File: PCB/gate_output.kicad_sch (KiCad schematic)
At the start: 7 parts

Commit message: :sparkles: Add the counter logic
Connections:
- net GATE_OUT: no longer D?.2 (A)
- net at Q?.3 (E), R?.1, R?.2: now also D?.2 (A)
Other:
- moved on the sheet: D?, R?

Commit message: :wrench: Set CLIFF footprints for the jacks
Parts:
- J?: footprint moPsy:Jack_3.5mm_QingPu_WQP-PJ398SM_Vertical_CircularHoles_Centered -> moPsy:CLIFF 3.5mm S6 Mono Jack Socket
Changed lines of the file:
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@@
       (effects (font (size 1.27 1.27)) (justify right))
     )
-    (property "Footprint" "moPsy:Jack_3.5mm_QingPu_WQP-PJ398SM_Vertical_CircularHoles_Centered" (at 92.075 63.5 0)
+    (property "Footprint" "moPsy:CLIFF 3.5mm S6 Mono Jack Socket" (at 92.075 63.5 0)
       (effects (font (size 1.27 1.27)) hide)
     )

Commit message: :wrench: Adjust project name on sheets
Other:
- company: (none) -> moPsy
- title: (none) -> DIV
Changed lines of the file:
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@@
 (kicad_sch (version 20230121) (generator eeschema)
   (paper "A4")
+  (title_block
+    (title "DIV")
+    (date "2023-04-03")
+    (rev "v1")
+    (company "moPsy")
+  )
   (junction (at 66.675 55.245) (diameter 0) (color 0 0 0 0)
   )
@@
         )
       )
-      (project "the-count"
+      (project "div"
         (path "/69636855-5bea-4b1f-bae0-d5724c7c5e69"
           (reference "Q?") (unit 1)
@@
         )
       )
-      (project "the-count"
+      (project "div"
         (path "/69636855-5bea-4b1f-bae0-d5724c7c5e69"
           (reference "R?") (unit 1)
@@
         )
       )
-      (project "the-count"
+      (project "div"
         (path "/69636855-5bea-4b1f-bae0-d5724c7c5e69"
           (reference "R?") (unit 1)
@@
         )
       )
-      (project "the-count"
+      (project "div"
         (path "/69636855-5bea-4b1f-bae0-d5724c7c5e69"
           (reference "#PWR?") (unit 1)
@@
         )
       )
-      (project "the-count"
+      (project "div"
         (path "/69636855-5bea-4b1f-bae0-d5724c7c5e69"
           (reference "R?") (unit 1)
@@
         )
       )
-      (project "the-count"
+      (project "div"
         (path "/69636855-5bea-4b1f-bae0-d5724c7c5e69"
           (reference "#PWR?") (unit 1)
@@
         )
       )
-      (project "the-count"
+      (project "div"
         (path "/69636855-5bea-4b1f-bae0-d5724c7c5e69"
           (reference "R?") (unit 1)
@@
         )
       )
-      (project "the-count"
+      (project "div"
         (path "/69636855-5bea-4b1f-bae0-d5724c7c5e69"
           (reference "#PWR?") (unit 1)
@@
         )
       )
-      (project "the-count"
+      (project "div"
         (path "/69636855-5bea-4b1f-bae0-d5724c7c5e69"
           (reference "D?") (unit 1)
@@
         )
       )
-      (project "the-count"
+      (project "div"
         (path "/69636855-5bea-4b1f-bae0-d5724c7c5e69"
           (reference "J?") (unit 1)
@@
         )
       )
-      (project "the-count"
-        (path "/69636855-5bea-4b1f-bae0-d5724c7c5e69"
-          (reference "#PWR?") (unit 1)
+      (project "div"
+        (path "/69636855-5bea-4b1f-bae0-d5724c7c5e69"
+          (reference "#PWR?") (unit 1)

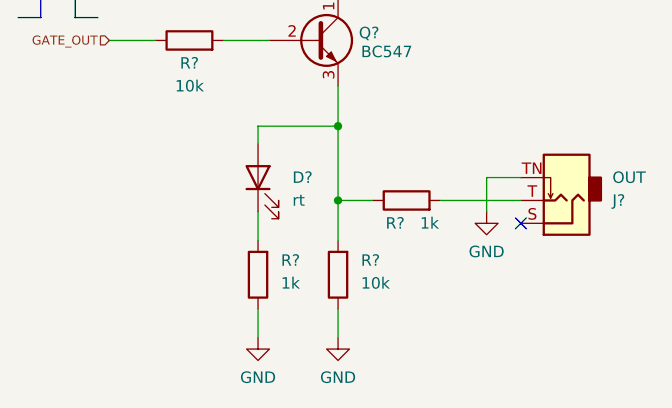
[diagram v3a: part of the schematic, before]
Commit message: :wrench: Adjust LED series resistors
With 4k7 the brightness is much better to look at.
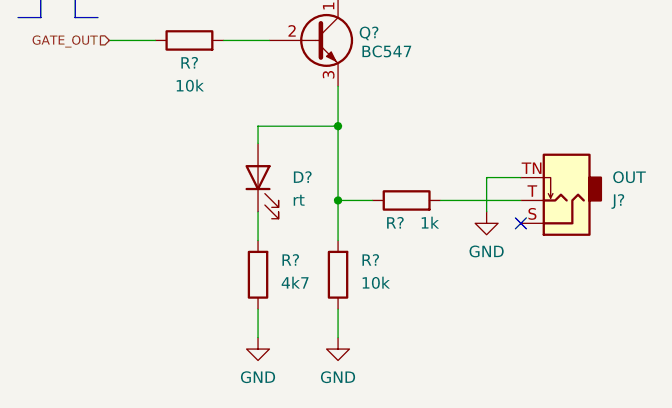
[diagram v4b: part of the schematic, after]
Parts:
- R?: value 1k -> 4k7
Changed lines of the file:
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@@
       (effects (font (size 1.27 1.27)) (justify right))
     )
-    (property "Value" "1k" (at 60.325 72.7075 0)
+    (property "Value" "4k7" (at 60.325 72.7075 0)
       (effects (font (size 1.27 1.27)) (justify right))
     )

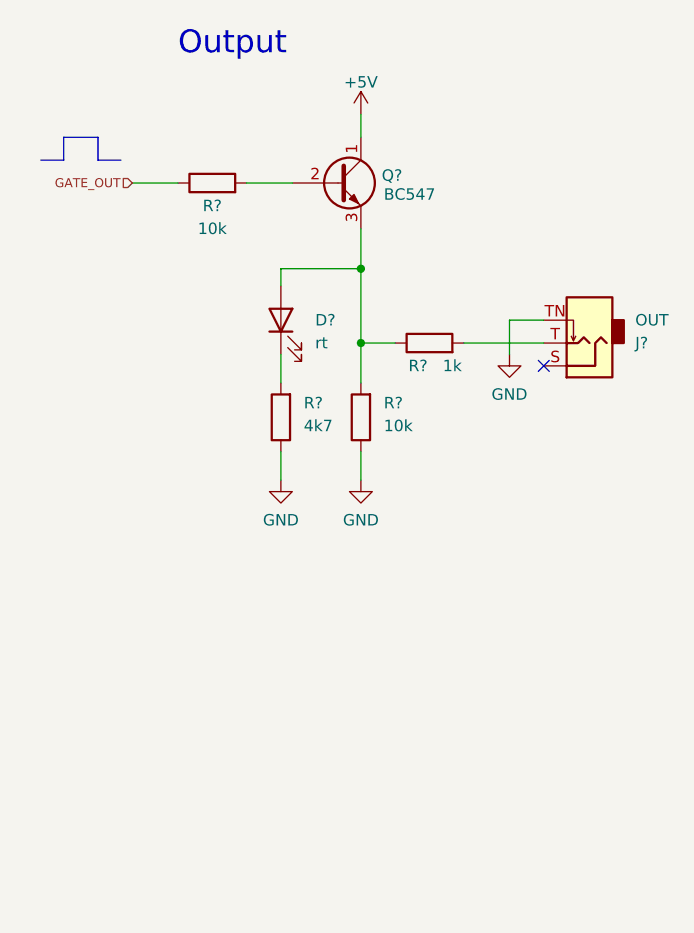
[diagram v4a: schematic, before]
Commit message: :hammer: Change output gate for 12V
Add a resistor divider to create about 5V for the gate output.
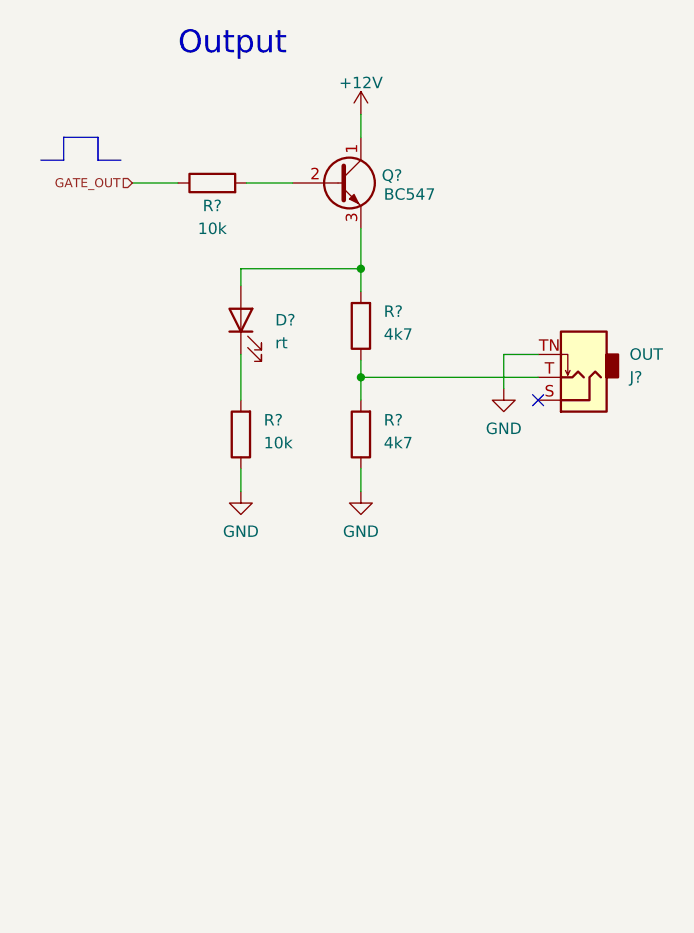
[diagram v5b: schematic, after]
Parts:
- removed R?: 1k, Resistor_THT:R_Axial_DIN0207_L6.3mm_D2.5mm_P7.62mm_Horizontal, symbol Device:R
- added R?: 4k7, Resistor_THT:R_Axial_DIN0207_L6.3mm_D2.5mm_P7.62mm_Horizontal, symbol Device:R
- R?: value 4k7 -> 10k
- R?: value 10k -> 4k7
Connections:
- net at D?.2 (A), Q?.3 (E): now also R?.2; no longer R?.2
- net at J?.T: now also R?.2, R?.1
- net +5V renamed +12V
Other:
- moved on the sheet: D?, J?, R?

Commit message: :art: Remove base resistor from output stage
The emitter follower does not need a base resistor.
Current has been measured at 11µA if the output is shorted to ground.
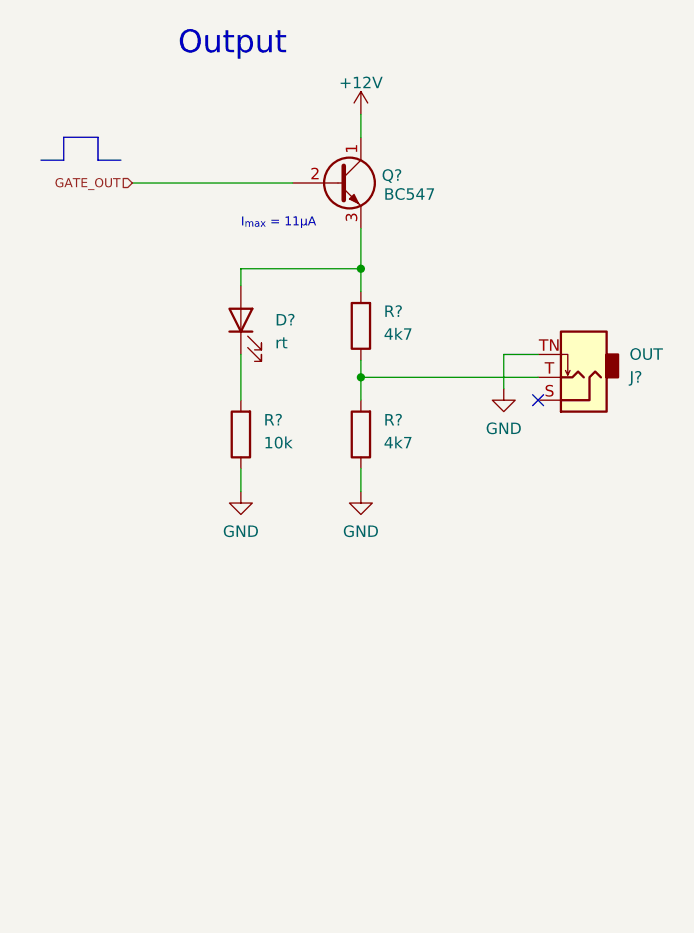
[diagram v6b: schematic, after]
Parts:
- removed R?: 10k, Resistor_THT:R_Axial_DIN0207_L6.3mm_D2.5mm_P7.62mm_Horizontal, symbol Device:R
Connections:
- net GATE_OUT: now also Q?.2 (B)
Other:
- note added: "I_{max} = 11µA"
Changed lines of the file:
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@@
     (stroke (width 0) (type solid))
-  )
-  (wire (pts (xy 53.975 45.72) (xy 59.055 45.72))
-    (stroke (width 0) (type default))
   )
   (polyline (pts (xy 33.655 43.18) (xy 31.115 43.18))
@@
     (stroke (width 0) (type default))
   )
-  (wire (pts (xy 41.275 45.72) (xy 46.355 45.72))
+  (wire (pts (xy 41.275 45.72) (xy 59.055 45.72))
     (stroke (width 0) (type default))
+  )
+  (text "I_{max} = 11µA" (at 53.34 50.8 0)
+    (effects (font (size 1 1)) (justify left bottom))
   )
   (text "Output" (at 46.355 31.75 0)
@@
         )
       )
-    )
-  )
-  (symbol (lib_id "Device:R") (at 50.165 45.72 90) (unit 1)
-    (in_bom yes) (on_board yes) (dnp no)
-    (property "Reference" "R?" (at 50.165 48.26 90)
-      (effects (font (size 1.27 1.27)))
-    )
-    (property "Value" "10k" (at 50.165 50.8 90)
-      (effects (font (size 1.27 1.27)))
-    )
-    (property "Footprint" "Resistor_THT:R_Axial_DIN0207_L6.3mm_D2.5mm_P7.62mm_Horizontal" (at 50.165 47.498 90)
-      (effects (font (size 1.27 1.27)) hide)
-    )
-    (property "Datasheet" "~" (at 50.165 45.72 0)
-      (effects (font (size 1.27 1.27)) hide)
-    )
-    (pin "1")
-    (pin "2")
-    (instances
-      (project "manual-gate-trigger-source"
-        (path "/64d6412c-bfad-42df-9ed7-bcc6cbff0470/5e147908-dd0e-44a6-bf7b-e0f4f3b88ce0"
-          (reference "R?") (unit 1)
-        )
-        (path "/64d6412c-bfad-42df-9ed7-bcc6cbff0470/4d130511-3de2-468d-9ad3-9fd4dd47645e"
-          (reference "R?") (unit 1)
-        )
-        (path "/64d6412c-bfad-42df-9ed7-bcc6cbff0470/b83b5c1b-da69-40b5-857e-949eb4f1eab8"
-          (reference "R?") (unit 1)
-        )
-        (path "/64d6412c-bfad-42df-9ed7-bcc6cbff0470/b0ca186f-8794-49d8-ae6e-2d447887c3e3"
-          (reference "R?") (unit 1)
-        )
-      )
-      (project "div"
-        (path "/69636855-5bea-4b1f-bae0-d5724c7c5e69"
-          (reference "R?") (unit 1)
-        )
-        (path "/69636855-5bea-4b1f-bae0-d5724c7c5e69/ddb23b62-aa27-4614-8e08-b908b2a2dd99"
-          (reference "R?") (unit 1)
-        )
-        (path "/69636855-5bea-4b1f-bae0-d5724c7c5e69/61f4bdd8-3e4f-4e0c-a5fa-951e97fb38b8"
-          (reference "R?") (unit 1)
-        )
-        (path "/69636855-5bea-4b1f-bae0-d5724c7c5e69/d48a94fa-bfe1-4bce-a3d7-937659f4df9e"
-          (reference "R?") (unit 1)
-        )
-        (path "/69636855-5bea-4b1f-bae0-d5724c7c5e69/e2f85f9a-c5ab-41b2-b8ce-b63f382b5258"
-          (reference "R?") (unit 1)
-        )
-        (path "/69636855-5bea-4b1f-bae0-d5724c7c5e69/301a9e1d-1dbb-4a63-a88b-1d93e257644e"
-          (reference "R?") (unit 1)
-        )
-        (path "/69636855-5bea-4b1f-bae0-d5724c7c5e69/82e60134-6463-4f35-8227-ac1dc3c9b002"
-          (reference "R?") (unit 1)
-        )
-      )

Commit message: :hammer: Optimize schematic for PCB layout
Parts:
- D?: value rt -> gn
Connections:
- net GND: now also J?.S; no longer J?.TN
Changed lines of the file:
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@@
   (junction (at 66.675 67.31) (diameter 0) (color 0 0 0 0)
   )
-  (no_connect (at 86.36 69.85))
+  (no_connect (at 86.36 64.77))
   (wire (pts (xy 66.675 38.1) (xy 66.675 40.64))
     (stroke (width 0) (type default))
@@
     (stroke (width 0) (type solid))
   )
+  (wire (pts (xy 82.55 69.85) (xy 82.55 71.12))
+    (stroke (width 0) (type default))
+  )
   (polyline (pts (xy 33.655 43.18) (xy 31.115 43.18))
     (stroke (width 0) (type solid))
   )
-  (wire (pts (xy 82.55 64.77) (xy 82.55 68.58))
-    (stroke (width 0) (type default))
-  )
   (wire (pts (xy 53.34 77.47) (xy 53.34 80.01))
-    (stroke (width 0) (type default))
-  )
-  (wire (pts (xy 82.55 64.77) (xy 86.36 64.77))
     (stroke (width 0) (type default))
   )
@@
   )
   (wire (pts (xy 66.675 65.405) (xy 66.675 67.31))
+    (stroke (width 0) (type default))
+  )
+  (wire (pts (xy 86.36 69.85) (xy 82.55 69.85))
     (stroke (width 0) (type default))
   )
@@
       (effects (font (size 1.27 1.27)) (justify right))
     )
-    (property "Value" "rt" (at 57.15 63.5 90)
+    (property "Value" "gn" (at 57.15 63.5 90)
       (effects (font (size 1.27 1.27)) (justify right))
     )
@@
     )
   )
-  (symbol (lib_id "power:GND") (at 82.55 68.58 0) (unit 1)
+  (symbol (lib_id "power:GND") (at 82.55 71.12 0) (unit 1)
     (in_bom yes) (on_board yes) (dnp no) (fields_autoplaced)
-    (property "Reference" "#PWR?" (at 82.55 74.93 0)
-      (effects (font (size 1.27 1.27)) hide)
-    )
-    (property "Value" "GND" (at 82.55 73.0234 0)
+    (property "Reference" "#PWR?" (at 82.55 77.47 0)
+      (effects (font (size 1.27 1.27)) hide)
+    )
+    (property "Value" "GND" (at 82.55 75.5634 0)
       (effects (font (size 1.27 1.27)))
     )
-    (property "Footprint" "" (at 82.55 68.58 0)
-      (effects (font (size 1.27 1.27)) hide)
-    )
-    (property "Datasheet" "" (at 82.55 68.58 0)
-      (effects (font (size 1.27 1.27)) hide)
-    )
+    (property "Footprint" "" (at 82.55 71.12 0)
+      (effects (font (size 1.27 1.27)) hide)
+    )
+    (property "Datasheet" "" (at 82.55 71.12 0)
+      (effects (font (size 1.27 1.27)) hide)
+    )
